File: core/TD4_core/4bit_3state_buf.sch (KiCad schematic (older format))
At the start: 6 parts

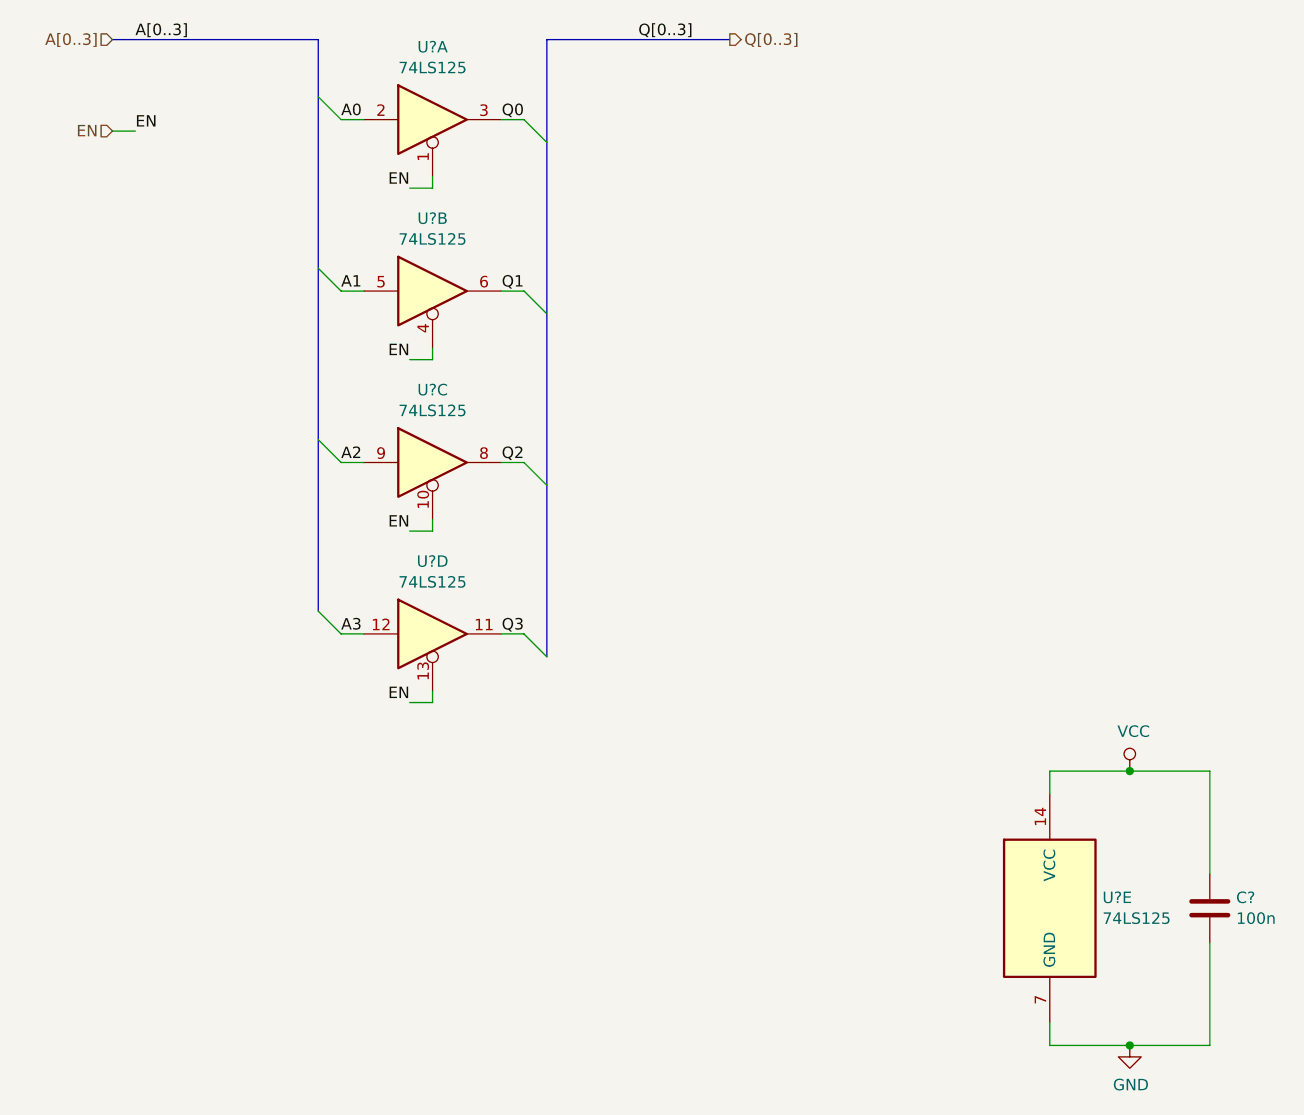
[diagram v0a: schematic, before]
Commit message: Core assembled; decoder left
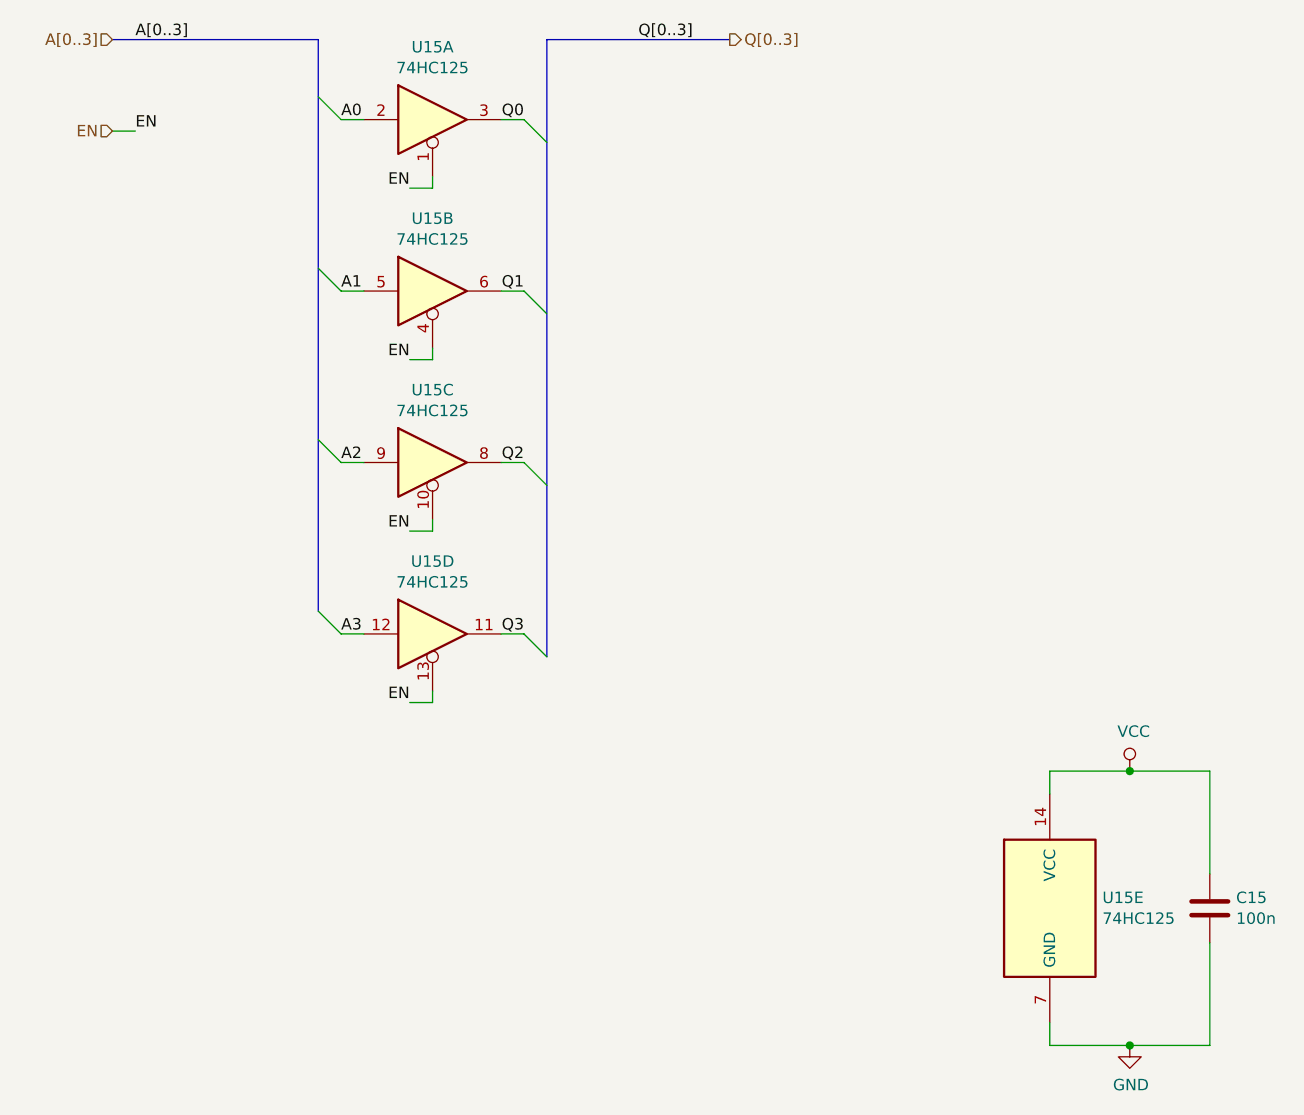
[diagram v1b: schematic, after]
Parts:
- U15: renamed from U?; value 74LS125 -> 74HC125
- gave numbers to parts that had none: 1
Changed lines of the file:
@@
 $Descr A4 11693 8268
 encoding utf-8
-Sheet 9 9
+Sheet 8 9
 Title ""
 Date ""
@@
 $EndDescr
 $Comp
-L 74xx:74LS125 U?
+L 74xx:74LS125 U15
 U 1 1 5C662A4F
 P 5600 2250
-F 0 "U?" H 5600 2567 50  0000 C CNN
-F 1 "74LS125" H 5600 2476 50  0000 C CNN
+F 0 "U15" H 5600 2567 50  0000 C CNN
+F 1 "74HC125" H 5600 2476 50  0000 C CNN
 F 2 "" H 5600 2250 50  0001 C CNN
 F 3 "http://www.ti.com/lit/gpn/sn74LS125" H 5600 2250 50  0001 C CNN
@@
 $EndComp
 $Comp
-L 74xx:74LS125 U?
+L 74xx:74LS125 U15
 U 2 1 5C662AA5
 P 5600 3000
-F 0 "U?" H 5600 3317 50  0000 C CNN
-F 1 "74LS125" H 5600 3226 50  0000 C CNN
+F 0 "U15" H 5600 3317 50  0000 C CNN
+F 1 "74HC125" H 5600 3226 50  0000 C CNN
 F 2 "" H 5600 3000 50  0001 C CNN
 F 3 "http://www.ti.com/lit/gpn/sn74LS125" H 5600 3000 50  0001 C CNN
@@
 $EndComp
 $Comp
-L 74xx:74LS125 U?
+L 74xx:74LS125 U15
 U 3 1 5C662AD3
 P 5600 3750
-F 0 "U?" H 5600 4067 50  0000 C CNN
-F 1 "74LS125" H 5600 3976 50  0000 C CNN
+F 0 "U15" H 5600 4067 50  0000 C CNN
+F 1 "74HC125" H 5600 3976 50  0000 C CNN
 F 2 "" H 5600 3750 50  0001 C CNN
 F 3 "http://www.ti.com/lit/gpn/sn74LS125" H 5600 3750 50  0001 C CNN
@@
 $EndComp
 $Comp
-L 74xx:74LS125 U?
+L 74xx:74LS125 U15
 U 4 1 5C662B05
 P 5600 4500
-F 0 "U?" H 5600 4817 50  0000 C CNN
-F 1 "74LS125" H 5600 4726 50  0000 C CNN
+F 0 "U15" H 5600 4817 50  0000 C CNN
+F 1 "74HC125" H 5600 4726 50  0000 C CNN
 F 2 "" H 5600 4500 50  0001 C CNN
 F 3 "http://www.ti.com/lit/gpn/sn74LS125" H 5600 4500 50  0001 C CNN
@@
 $EndComp
 $Comp
-L 74xx:74LS125 U?
+L 74xx:74LS125 U15
 U 5 1 5C662B31
 P 8300 5700
-F 0 "U?" H 8530 5746 50  0000 L CNN
-F 1 "74LS125" H 8530 5655 50  0000 L CNN
+F 0 "U15" H 8530 5746 50  0000 L CNN
+F 1 "74HC125" H 8530 5655 50  0000 L CNN
 F 2 "" H 8300 5700 50  0001 C CNN
 F 3 "http://www.ti.com/lit/gpn/sn74LS125" H 8300 5700 50  0001 C CNN
@@
 Q3
 $Comp
-L Device:C C?
+L Device:C C15
 U 1 1 5C6652A0
 P 9000 5700
-F 0 "C?" H 9115 5746 50  0000 L CNN
+F 0 "C15" H 9115 5746 50  0000 L CNN
 F 1 "100n" H 9115 5655 50  0000 L CNN
 F 2 "" H 9038 5550 50  0001 C CNN
@@
 	9000 6300 9000 5850
 $Comp
-L power:VCC #PWR?
+L power:VCC #PWR0132
 U 1 1 5C6657D0
 P 8650 5100
-F 0 "#PWR?" H 8650 4950 50  0001 C CNN
+F 0 "#PWR0132" H 8650 4950 50  0001 C CNN
 F 1 "VCC" H 8667 5273 50  0000 C CNN
 F 2 "" H 8650 5100 50  0001 C CNN
@@
 	8650 5100 9000 5100
 $Comp
-L power:GND #PWR?
+L power:GND #PWR0133
 U 1 1 5C66581B
 P 8650 6300
-F 0 "#PWR?" H 8650 6050 50  0001 C CNN
+F 0 "#PWR0133" H 8650 6050 50  0001 C CNN
 F 1 "GND" H 8655 6127 50  0000 C CNN
 F 2 "" H 8650 6300 50  0001 C CNN
@@
 Wire Wire Line
 	4200 2300 4300 2300
+Text Label 4300 2300 0    50   ~ 0
+EN
 Wire Bus Line
 	5100 1900 5100 4400
 Wire Bus Line
 	6100 1900 6100 4600
-Text Label 4300 2300 0    50   ~ 0
-EN
 $EndSCHEMATC

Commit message: Decoder done (finally!)
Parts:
- renumbered C15 to C34, U15 to U34
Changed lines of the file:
@@
 $Descr A4 11693 8268
 encoding utf-8
-Sheet 8 9
+Sheet 8 23
 Title ""
 Date ""
@@
 $EndDescr
 $Comp
-L 74xx:74LS125 U15
+L 74xx:74LS125 U34
 U 1 1 5C662A4F
 P 5600 2250
-F 0 "U15" H 5600 2567 50  0000 C CNN
+F 0 "U34" H 5600 2567 50  0000 C CNN
 F 1 "74HC125" H 5600 2476 50  0000 C CNN
 F 2 "" H 5600 2250 50  0001 C CNN
@@
 $EndComp
 $Comp
-L 74xx:74LS125 U15
+L 74xx:74LS125 U34
 U 2 1 5C662AA5
 P 5600 3000
-F 0 "U15" H 5600 3317 50  0000 C CNN
+F 0 "U34" H 5600 3317 50  0000 C CNN
 F 1 "74HC125" H 5600 3226 50  0000 C CNN
 F 2 "" H 5600 3000 50  0001 C CNN
@@
 $EndComp
 $Comp
-L 74xx:74LS125 U15
+L 74xx:74LS125 U34
 U 3 1 5C662AD3
 P 5600 3750
-F 0 "U15" H 5600 4067 50  0000 C CNN
+F 0 "U34" H 5600 4067 50  0000 C CNN
 F 1 "74HC125" H 5600 3976 50  0000 C CNN
 F 2 "" H 5600 3750 50  0001 C CNN
@@
 $EndComp
 $Comp
-L 74xx:74LS125 U15
+L 74xx:74LS125 U34
 U 4 1 5C662B05
 P 5600 4500
-F 0 "U15" H 5600 4817 50  0000 C CNN
+F 0 "U34" H 5600 4817 50  0000 C CNN
 F 1 "74HC125" H 5600 4726 50  0000 C CNN
 F 2 "" H 5600 4500 50  0001 C CNN
@@
 $EndComp
 $Comp
-L 74xx:74LS125 U15
+L 74xx:74LS125 U34
 U 5 1 5C662B31
 P 8300 5700
-F 0 "U15" H 8530 5746 50  0000 L CNN
+F 0 "U34" H 8530 5746 50  0000 L CNN
 F 1 "74HC125" H 8530 5655 50  0000 L CNN
 F 2 "" H 8300 5700 50  0001 C CNN
@@
 Q3
 $Comp
-L Device:C C15
+L Device:C C34
 U 1 1 5C6652A0
 P 9000 5700
-F 0 "C15" H 9115 5746 50  0000 L CNN
+F 0 "C34" H 9115 5746 50  0000 L CNN
 F 1 "100n" H 9115 5655 50  0000 L CNN
 F 2 "" H 9038 5550 50  0001 C CNN
@@
 	9000 6300 9000 5850
 $Comp
-L power:VCC #PWR0132
+L power:VCC #PWR0113
 U 1 1 5C6657D0
 P 8650 5100
-F 0 "#PWR0132" H 8650 4950 50  0001 C CNN
+F 0 "#PWR0113" H 8650 4950 50  0001 C CNN
 F 1 "VCC" H 8667 5273 50  0000 C CNN
 F 2 "" H 8650 5100 50  0001 C CNN
@@
 	8650 5100 9000 5100
 $Comp
-L power:GND #PWR0133
+L power:GND #PWR0114
 U 1 1 5C66581B
 P 8650 6300
-F 0 "#PWR0133" H 8650 6050 50  0001 C CNN
+F 0 "#PWR0114" H 8650 6050 50  0001 C CNN
 F 1 "GND" H 8655 6127 50  0000 C CNN
 F 2 "" H 8650 6300 50  0001 C CNN

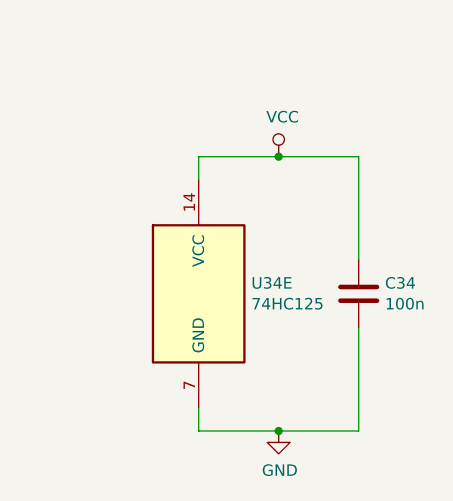
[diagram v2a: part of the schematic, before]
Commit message: Core schematic done. Backplane connector added, including separate .sch file to append.
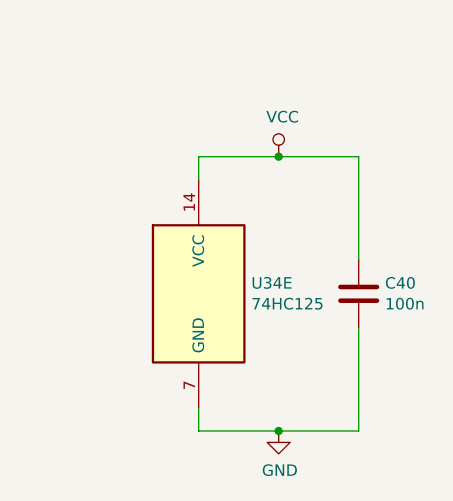
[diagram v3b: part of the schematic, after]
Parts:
- C40: renamed from C34; footprint (none) -> Capacitor_SMD:C_0805_2012Metric
- U34: footprint (none) -> Package_SO:SOIC-14_3.9x8.7mm_P1.27mm
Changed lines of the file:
@@
 encoding utf-8
 Sheet 8 23
-Title ""
+Title "TD4 core module"
 Date ""
-Rev ""
+Rev "v1.0"
 Comp ""
 Comment1 ""
@@
 F 0 "U34" H 5600 2567 50  0000 C CNN
 F 1 "74HC125" H 5600 2476 50  0000 C CNN
-F 2 "" H 5600 2250 50  0001 C CNN
+F 2 "Package_SO:SOIC-14_3.9x8.7mm_P1.27mm" H 5600 2250 50  0001 C CNN
 F 3 "http://www.ti.com/lit/gpn/sn74LS125" H 5600 2250 50  0001 C CNN
 	1    5600 2250
@@
 F 0 "U34" H 5600 3317 50  0000 C CNN
 F 1 "74HC125" H 5600 3226 50  0000 C CNN
-F 2 "" H 5600 3000 50  0001 C CNN
+F 2 "Package_SO:SOIC-14_3.9x8.7mm_P1.27mm" H 5600 3000 50  0001 C CNN
 F 3 "http://www.ti.com/lit/gpn/sn74LS125" H 5600 3000 50  0001 C CNN
 	2    5600 3000
@@
 F 0 "U34" H 5600 4067 50  0000 C CNN
 F 1 "74HC125" H 5600 3976 50  0000 C CNN
-F 2 "" H 5600 3750 50  0001 C CNN
+F 2 "Package_SO:SOIC-14_3.9x8.7mm_P1.27mm" H 5600 3750 50  0001 C CNN
 F 3 "http://www.ti.com/lit/gpn/sn74LS125" H 5600 3750 50  0001 C CNN
 	3    5600 3750
@@
 F 0 "U34" H 5600 4817 50  0000 C CNN
 F 1 "74HC125" H 5600 4726 50  0000 C CNN
-F 2 "" H 5600 4500 50  0001 C CNN
+F 2 "Package_SO:SOIC-14_3.9x8.7mm_P1.27mm" H 5600 4500 50  0001 C CNN
 F 3 "http://www.ti.com/lit/gpn/sn74LS125" H 5600 4500 50  0001 C CNN
 	4    5600 4500
@@
 F 0 "U34" H 8530 5746 50  0000 L CNN
 F 1 "74HC125" H 8530 5655 50  0000 L CNN
-F 2 "" H 8300 5700 50  0001 C CNN
+F 2 "Package_SO:SOIC-14_3.9x8.7mm_P1.27mm" H 8300 5700 50  0001 C CNN
 F 3 "http://www.ti.com/lit/gpn/sn74LS125" H 8300 5700 50  0001 C CNN
 	5    8300 5700
@@
 Q3
 $Comp
-L Device:C C34
+L Device:C C40
 U 1 1 5C6652A0
 P 9000 5700
-F 0 "C34" H 9115 5746 50  0000 L CNN
+F 0 "C40" H 9115 5746 50  0000 L CNN
 F 1 "100n" H 9115 5655 50  0000 L CNN
-F 2 "" H 9038 5550 50  0001 C CNN
+F 2 "Capacitor_SMD:C_0805_2012Metric" H 9038 5550 50  0001 C CNN
 F 3 "~" H 9000 5700 50  0001 C CNN
 	1    9000 5700
@@
 	9000 6300 9000 5850
 $Comp
-L power:VCC #PWR0113
+L power:VCC #PWR0127
 U 1 1 5C6657D0
 P 8650 5100
-F 0 "#PWR0113" H 8650 4950 50  0001 C CNN
+F 0 "#PWR0127" H 8650 4950 50  0001 C CNN
 F 1 "VCC" H 8667 5273 50  0000 C CNN
 F 2 "" H 8650 5100 50  0001 C CNN
@@
 	8650 5100 9000 5100
 $Comp
-L power:GND #PWR0114
+L power:GND #PWR0128
 U 1 1 5C66581B
 P 8650 6300
-F 0 "#PWR0114" H 8650 6050 50  0001 C CNN
+F 0 "#PWR0128" H 8650 6050 50  0001 C CNN
 F 1 "GND" H 8655 6127 50  0000 C CNN
 F 2 "" H 8650 6300 50  0001 C CNN

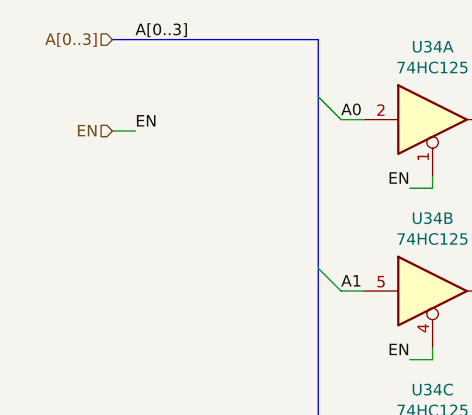
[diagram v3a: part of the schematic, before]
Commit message: Added debug headers to core
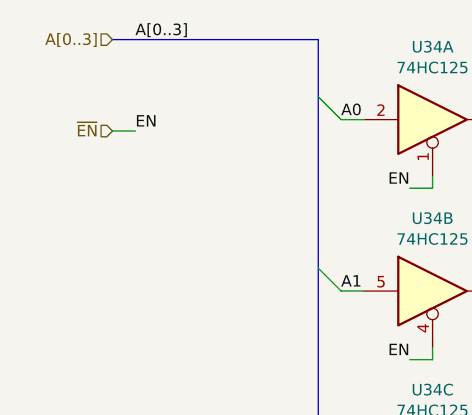
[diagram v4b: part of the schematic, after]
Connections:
- net EN renamed ~EN
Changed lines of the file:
@@
 $Descr A4 11693 8268
 encoding utf-8
-Sheet 8 23
+Sheet 21 30
 Title "TD4 core module"
 Date ""
@@
 U 1 1 5C662A4F
 P 5600 2250
+AR Path="/5C6628C5/5C662A4F" Ref="U34"  Part="1"
+AR Path="/5C6C9696/5C662A4F" Ref="U?"  Part="1"
+AR Path="/5C6CE91F/5C662A4F" Ref="U?"  Part="1"
+AR Path="/5C72E552/5C7339DC/5C662A4F" Ref="U?"  Part="1"
+AR Path="/5C74C5C4/5C7339DC/5C662A4F" Ref="U?"  Part="1"
+AR Path="/5C758048/5C7339DC/5C662A4F" Ref="U?"  Part="1"
+AR Path="/5C77FFF0/5C780016/5C7339DC/5C662A4F" Ref="U?"  Part="1"
 F 0 "U34" H 5600 2567 50  0000 C CNN
 F 1 "74HC125" H 5600 2476 50  0000 C CNN
@@
 U 2 1 5C662AA5
 P 5600 3000
+AR Path="/5C6628C5/5C662AA5" Ref="U34"  Part="2"
+AR Path="/5C6C9696/5C662AA5" Ref="U?"  Part="2"
+AR Path="/5C6CE91F/5C662AA5" Ref="U?"  Part="2"
+AR Path="/5C72E552/5C7339DC/5C662AA5" Ref="U?"  Part="2"
+AR Path="/5C74C5C4/5C7339DC/5C662AA5" Ref="U?"  Part="2"
+AR Path="/5C758048/5C7339DC/5C662AA5" Ref="U?"  Part="2"
+AR Path="/5C77FFF0/5C780016/5C7339DC/5C662AA5" Ref="U?"  Part="2"
 F 0 "U34" H 5600 3317 50  0000 C CNN
 F 1 "74HC125" H 5600 3226 50  0000 C CNN
@@
 U 3 1 5C662AD3
 P 5600 3750
+AR Path="/5C6628C5/5C662AD3" Ref="U34"  Part="3"
+AR Path="/5C6C9696/5C662AD3" Ref="U?"  Part="3"
+AR Path="/5C6CE91F/5C662AD3" Ref="U?"  Part="3"
+AR Path="/5C72E552/5C7339DC/5C662AD3" Ref="U?"  Part="3"
+AR Path="/5C74C5C4/5C7339DC/5C662AD3" Ref="U?"  Part="3"
+AR Path="/5C758048/5C7339DC/5C662AD3" Ref="U?"  Part="3"
+AR Path="/5C77FFF0/5C780016/5C7339DC/5C662AD3" Ref="U?"  Part="3"
 F 0 "U34" H 5600 4067 50  0000 C CNN
 F 1 "74HC125" H 5600 3976 50  0000 C CNN
@@
 U 4 1 5C662B05
 P 5600 4500
+AR Path="/5C6628C5/5C662B05" Ref="U34"  Part="4"
+AR Path="/5C6C9696/5C662B05" Ref="U?"  Part="4"
+AR Path="/5C6CE91F/5C662B05" Ref="U?"  Part="4"
+AR Path="/5C72E552/5C7339DC/5C662B05" Ref="U?"  Part="4"
+AR Path="/5C74C5C4/5C7339DC/5C662B05" Ref="U?"  Part="4"
+AR Path="/5C758048/5C7339DC/5C662B05" Ref="U?"  Part="4"
+AR Path="/5C77FFF0/5C780016/5C7339DC/5C662B05" Ref="U?"  Part="4"
 F 0 "U34" H 5600 4817 50  0000 C CNN
 F 1 "74HC125" H 5600 4726 50  0000 C CNN
@@
 U 5 1 5C662B31
 P 8300 5700
+AR Path="/5C6628C5/5C662B31" Ref="U34"  Part="5"
+AR Path="/5C6C9696/5C662B31" Ref="U?"  Part="5"
+AR Path="/5C6CE91F/5C662B31" Ref="U?"  Part="5"
+AR Path="/5C72E552/5C7339DC/5C662B31" Ref="U?"  Part="5"
+AR Path="/5C74C5C4/5C7339DC/5C662B31" Ref="U?"  Part="5"
+AR Path="/5C758048/5C7339DC/5C662B31" Ref="U?"  Part="5"
+AR Path="/5C77FFF0/5C780016/5C7339DC/5C662B31" Ref="U?"  Part="5"
 F 0 "U34" H 8530 5746 50  0000 L CNN
 F 1 "74HC125" H 8530 5655 50  0000 L CNN
@@
 U 1 1 5C6652A0
 P 9000 5700
+AR Path="/5C6628C5/5C6652A0" Ref="C40"  Part="1"
+AR Path="/5C6C9696/5C6652A0" Ref="C?"  Part="1"
+AR Path="/5C6CE91F/5C6652A0" Ref="C?"  Part="1"
+AR Path="/5C72E552/5C7339DC/5C6652A0" Ref="C?"  Part="1"
+AR Path="/5C74C5C4/5C7339DC/5C6652A0" Ref="C?"  Part="1"
+AR Path="/5C758048/5C7339DC/5C6652A0" Ref="C?"  Part="1"
+AR Path="/5C77FFF0/5C780016/5C7339DC/5C6652A0" Ref="C?"  Part="1"
 F 0 "C40" H 9115 5746 50  0000 L CNN
 F 1 "100n" H 9115 5655 50  0000 L CNN
@@
 U 1 1 5C6657D0
 P 8650 5100
+AR Path="/5C6628C5/5C6657D0" Ref="#PWR0127"  Part="1"
+AR Path="/5C6C9696/5C6657D0" Ref="#PWR?"  Part="1"
+AR Path="/5C6CE91F/5C6657D0" Ref="#PWR?"  Part="1"
+AR Path="/5C72E552/5C7339DC/5C6657D0" Ref="#PWR?"  Part="1"
+AR Path="/5C74C5C4/5C7339DC/5C6657D0" Ref="#PWR?"  Part="1"
+AR Path="/5C758048/5C7339DC/5C6657D0" Ref="#PWR?"  Part="1"
+AR Path="/5C77FFF0/5C780016/5C7339DC/5C6657D0" Ref="#PWR?"  Part="1"
 F 0 "#PWR0127" H 8650 4950 50  0001 C CNN
 F 1 "VCC" H 8667 5273 50  0000 C CNN
@@
 U 1 1 5C66581B
 P 8650 6300
+AR Path="/5C6628C5/5C66581B" Ref="#PWR0128"  Part="1"
+AR Path="/5C6C9696/5C66581B" Ref="#PWR?"  Part="1"
+AR Path="/5C6CE91F/5C66581B" Ref="#PWR?"  Part="1"
+AR Path="/5C72E552/5C7339DC/5C66581B" Ref="#PWR?"  Part="1"
+AR Path="/5C74C5C4/5C7339DC/5C66581B" Ref="#PWR?"  Part="1"
+AR Path="/5C758048/5C7339DC/5C66581B" Ref="#PWR?"  Part="1"
+AR Path="/5C77FFF0/5C780016/5C7339DC/5C66581B" Ref="#PWR?"  Part="1"
 F 0 "#PWR0128" H 8650 6050 50  0001 C CNN
 F 1 "GND" H 8655 6127 50  0000 C CNN
@@
 Q[0..3]
 Text HLabel 4200 2300 0    50   Input ~ 0
-EN
+~EN
 Wire Wire Line
 	4200 2300 4300 2300
